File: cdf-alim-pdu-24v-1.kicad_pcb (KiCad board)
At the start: 2 copper layers, 85 x 60 mm, 130 parts, among them J1 Conn_01x02, J10 Conn_01x02, J11 Conn_01x02, J12 Conn_01x02, J13 Conn_01x02, J14 Conn_01x02, J15 Conn_01x02, J16 Conn_01x02, J17 Conn_01x02, J2 Conn_01x02, J3 Conn_01x02, J4 Conn_01x02, J5 Conn_01x02, J6 Conn_01x02, J7 Conn_01x02, J8 Conn_01x02, J9 Conn_01x02, Q1 BSC019N04LS, Q2 BSC019N04LS, Q3 BSC019N04LS, U1 TPS25983, U2 TPS25983, U3 TPS25983, U4 HT753-1, U5 MX25947, U6 MX25947, U7 MX25947

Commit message: pcb: center board
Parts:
- moved C1 56.3 mm to (114.0, 104.2)
- moved C10 56.3 mm to (115.5, 112.0)
- moved C11 56.3 mm to (123.8, 102.8)
- moved C12 56.3 mm to (146.2, 120.5)
- moved C13 56.3 mm to (146.2, 73.8)
- moved C14 56.3 mm to (154.5, 111.2)
- moved C15 56.3 mm to (154.5, 64.5)
- moved C16 56.3 mm to (137.5, 65.0)
- moved C17 56.3 mm to (137.5, 120.0)
- moved C18 56.3 mm to (137.5, 73.0)
- moved C19 56.3 mm to (137.5, 112.0)
- moved C2 56.3 mm to (144.8, 112.8)
- moved C20 56.3 mm to (117.2, 116.0)
- moved C21 56.3 mm to (129.8, 79.0)
- moved C22 56.3 mm to (129.8, 106.0)
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
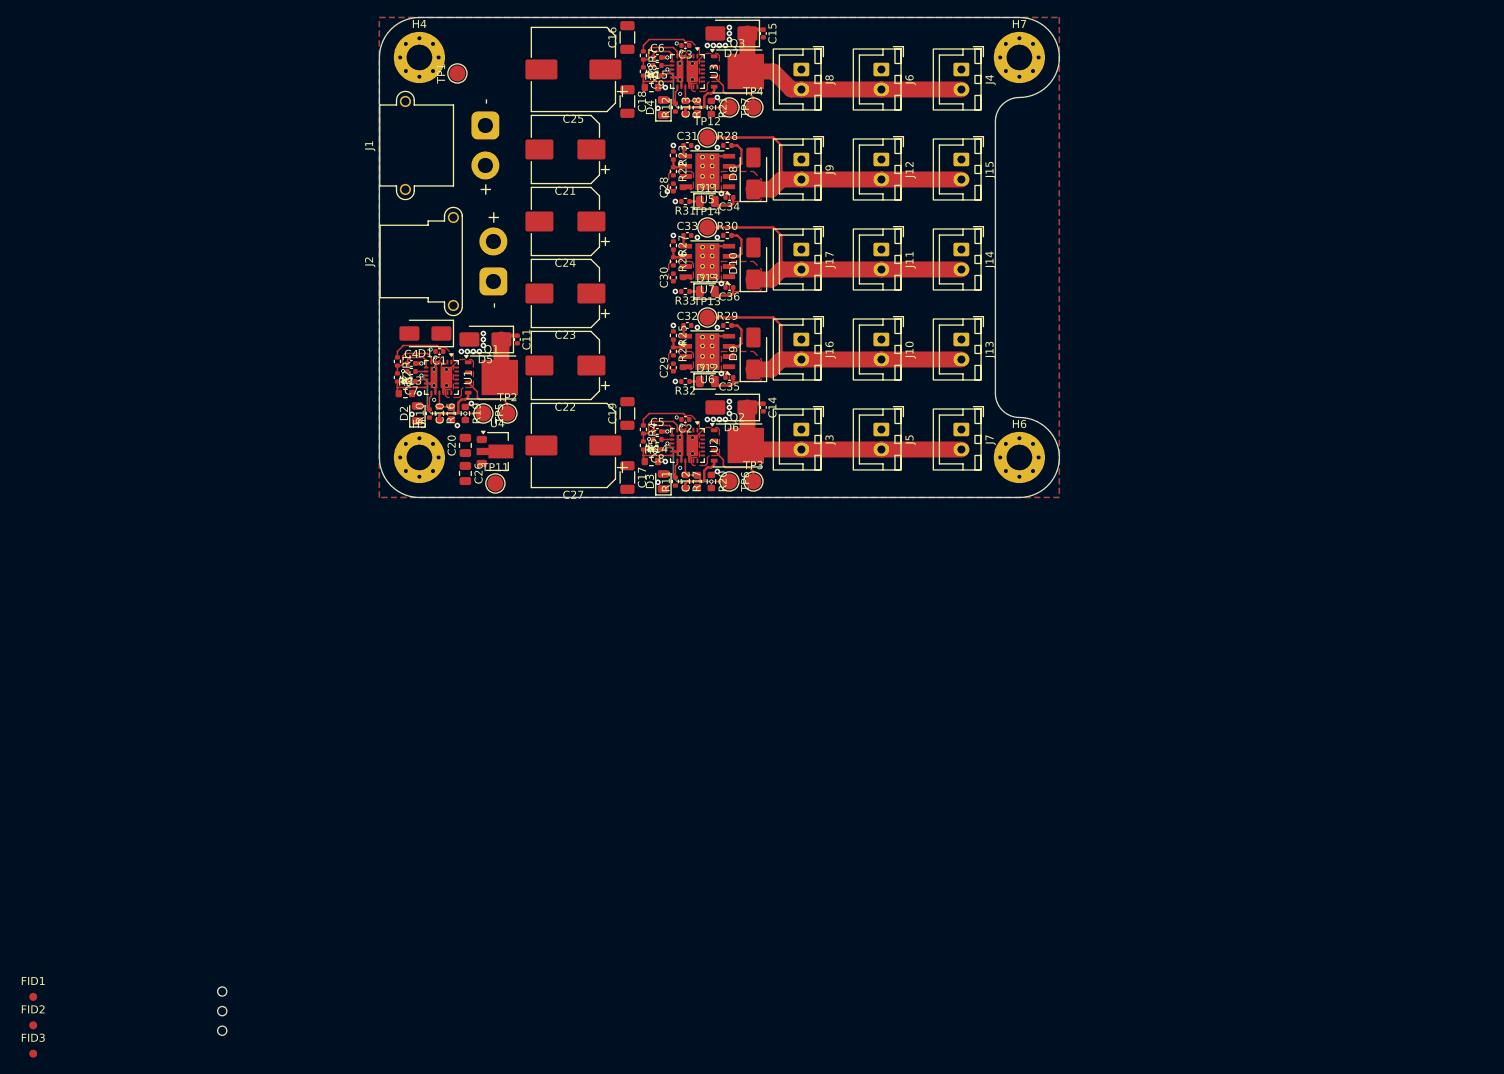
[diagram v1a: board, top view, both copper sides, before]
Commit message: pcb: place mounting holes/fiducials
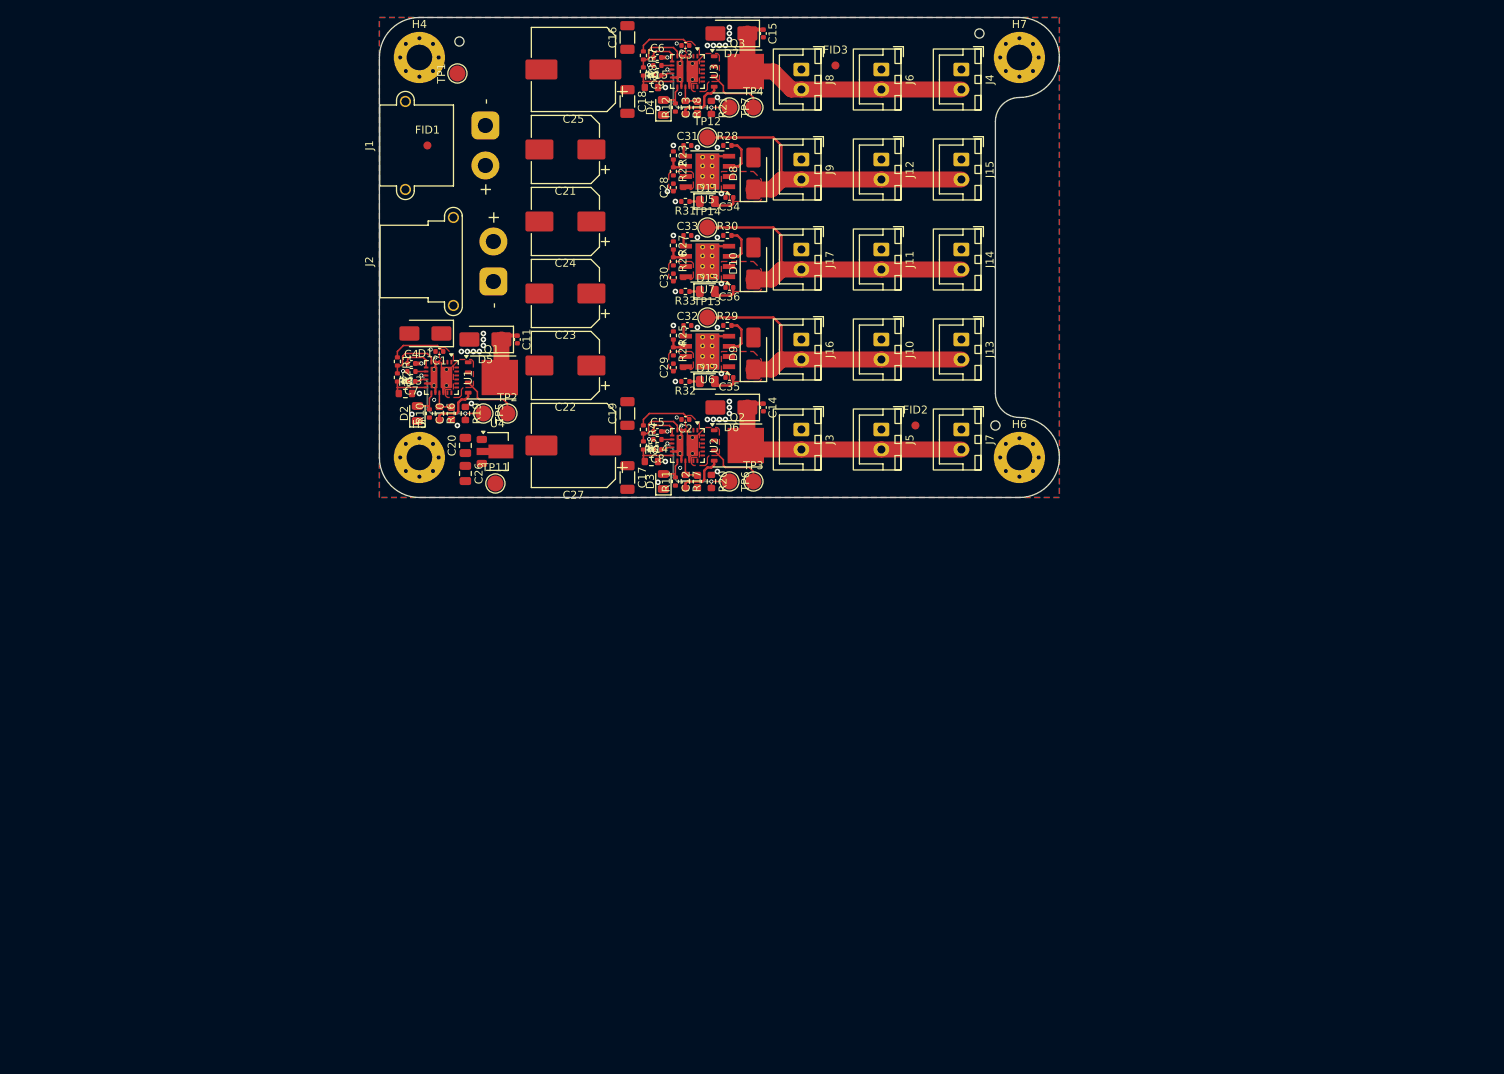
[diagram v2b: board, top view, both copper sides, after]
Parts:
- moved FID3 159.1 mm to (163.5, 68.5)
- moved H3 156.5 mm to (181.5, 64.5)
- moved FID2 133.3 mm to (173.5, 113.5)
- moved H2 124.8 mm to (116.5, 65.5)
- moved H1 119.8 mm to (183.5, 113.5)
- moved FID1 117.3 mm to (112.5, 78.5)
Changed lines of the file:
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@@
 	(footprint "Fiducial:Fiducial_1mm_Mask2mm"
 		(layer "F.Cu")
-		(at 63.225 184.925)
+		(at 112.5 78.5)
 		(descr "Fiducial, circular marking, 1mm bare copper, 2mm soldermask opening (Level A)")
 		(tags "fiducial")
@@
 	(footprint "Fiducial:Fiducial_1mm_Mask2mm"
 		(layer "F.Cu")
-		(at 63.225 192.025)
+		(at 163.5 68.5)
 		(descr "Fiducial, circular marking, 1mm bare copper, 2mm soldermask opening (Level A)")
 		(tags "fiducial")
@@
 	(footprint "MountingHole:ToolingHole_1.152mm"
 		(layer "F.Cu")
-		(at 86.855 184.255)
+		(at 183.5 113.5)
 		(descr "Tooling Hole 1.152mm, 1.3mm solder mask, JLCPCB specification, https://jlcpcb.com/help/article/How-to-add-tooling-holes-for-PCB-assembly-order")
 		(tags "mounting")
@@
 			(polygon
 				(pts
-					(xy 87.555 184.255) (xy 87.534659 184.087479) (xy 87.474819 183.929694) (xy 87.378958 183.790814)
-					(xy 87.252645 183.678911) (xy 87.103223 183.600489) (xy 86.939376 183.560104) (xy 86.770624 183.560104)
-					(xy 86.606777 183.600489) (xy 86.457355 183.678911) (xy 86.331042 183.790814) (xy 86.235181 183.929694)
-					(xy 86.175341 184.087479) (xy 86.155 184.255) (xy 86.175341 184.422521) (xy 86.235181 184.580306)
-					(xy 86.331042 184.719186) (xy 86.457355 184.831089) (xy 86.606777 184.909511) (xy 86.770624 184.949896)
-					(xy 86.939376 184.949896) (xy 87.103223 184.909511) (xy 87.252645 184.831089) (xy 87.378958 184.719186)
-					(xy 87.474819 184.580306) (xy 87.534659 184.422521)
+					(xy 184.2 113.5) (xy 184.179659 113.332479) (xy 184.119819 113.174694) (xy 184.023958 113.035814)
+					(xy 183.897645 112.923911) (xy 183.748223 112.845489) (xy 183.584376 112.805104) (xy 183.415624 112.805104)
+					(xy 183.251777 112.845489) (xy 183.102355 112.923911) (xy 182.976042 113.035814) (xy 182.880181 113.174694)
+					(xy 182.820341 113.332479) (xy 182.8 113.5) (xy 182.820341 113.667521) (xy 182.880181 113.825306)
+					(xy 182.976042 113.964186) (xy 183.102355 114.076089) (xy 183.251777 114.154511) (xy 183.415624 114.194896)
+					(xy 183.584376 114.194896) (xy 183.748223 114.154511) (xy 183.897645 114.076089) (xy 184.023958 113.964186)
+					(xy 184.119819 113.825306) (xy 184.179659 113.667521)
 				)
 			)
@@
 	(footprint "MountingHole:ToolingHole_1.152mm"
 		(layer "F.Cu")
-		(at 86.855 189.155)
+		(at 181.5 64.5)
 		(descr "Tooling Hole 1.152mm, 1.3mm solder mask, JLCPCB specification, https://jlcpcb.com/help/article/How-to-add-tooling-holes-for-PCB-assembly-order")
 		(tags "mounting")
@@
 			(polygon
 				(pts
-					(xy 87.555 189.155) (xy 87.534659 188.987479) (xy 87.474819 188.829694) (xy 87.378958 188.690814)
-					(xy 87.252645 188.578911) (xy 87.103223 188.500489) (xy 86.939376 188.460104) (xy 86.770624 188.460104)
-					(xy 86.606777 188.500489) (xy 86.457355 188.578911) (xy 86.331042 188.690814) (xy 86.235181 188.829694)
-					(xy 86.175341 188.987479) (xy 86.155 189.155) (xy 86.175341 189.322521) (xy 86.235181 189.480306)
-					(xy 86.331042 189.619186) (xy 86.457355 189.731089) (xy 86.606777 189.809511) (xy 86.770624 189.849896)
-					(xy 86.939376 189.849896) (xy 87.103223 189.809511) (xy 87.252645 189.731089) (xy 87.378958 189.619186)
-					(xy 87.474819 189.480306) (xy 87.534659 189.322521)
+					(xy 182.2 64.5) (xy 182.179659 64.332479) (xy 182.119819 64.174694) (xy 182.023958 64.035814) (xy 181.897645 63.923911)
+					(xy 181.748223 63.845489) (xy 181.584376 63.805104) (xy 181.415624 63.805104) (xy 181.251777 63.845489)
+					(xy 181.102355 63.923911) (xy 180.976042 64.035814) (xy 180.880181 64.174694) (xy 180.820341 64.332479)
+					(xy 180.8 64.5) (xy 180.820341 64.667521) (xy 180.880181 64.825306) (xy 180.976042 64.964186) (xy 181.102355 65.076089)
+					(xy 181.251777 65.154511) (xy 181.415624 65.194896) (xy 181.584376 65.194896) (xy 181.748223 65.154511)
+					(xy 181.897645 65.076089) (xy 182.023958 64.964186) (xy 182.119819 64.825306) (xy 182.179659 64.667521)
 				)
 			)
@@
 	(footprint "MountingHole:ToolingHole_1.152mm"
 		(layer "F.Cu")
-		(at 86.855 186.705)
+		(at 116.5 65.5)
 		(descr "Tooling Hole 1.152mm, 1.3mm solder mask, JLCPCB specification, https://jlcpcb.com/help/article/How-to-add-tooling-holes-for-PCB-assembly-order")
 		(tags "mounting")
@@
 			(polygon
 				(pts
-					(xy 87.555 186.705) (xy 87.534659 186.537479) (xy 87.474819 186.379694) (xy 87.378958 186.240814)
-					(xy 87.252645 186.128911) (xy 87.103223 186.050489) (xy 86.939376 186.010104) (xy 86.770624 186.010104)
-					(xy 86.606777 186.050489) (xy 86.457355 186.128911) (xy 86.331042 186.240814) (xy 86.235181 186.379694)
-					(xy 86.175341 186.537479) (xy 86.155 186.705) (xy 86.175341 186.872521) (xy 86.235181 187.030306)
-					(xy 86.331042 187.169186) (xy 86.457355 187.281089) (xy 86.606777 187.359511) (xy 86.770624 187.399896)
-					(xy 86.939376 187.399896) (xy 87.103223 187.359511) (xy 87.252645 187.281089) (xy 87.378958 187.169186)
-					(xy 87.474819 187.030306) (xy 87.534659 186.872521)
+					(xy 117.2 65.5) (xy 117.179659 65.332479) (xy 117.119819 65.174694) (xy 117.023958 65.035814) (xy 116.897645 64.923911)
+					(xy 116.748223 64.845489) (xy 116.584376 64.805104) (xy 116.415624 64.805104) (xy 116.251777 64.845489)
+					(xy 116.102355 64.923911) (xy 115.976042 65.035814) (xy 115.880181 65.174694) (xy 115.820341 65.332479)
+					(xy 115.8 65.5) (xy 115.820341 65.667521) (xy 115.880181 65.825306) (xy 115.976042 65.964186) (xy 116.102355 66.076089)
+					(xy 116.251777 66.154511) (xy 116.415624 66.194896) (xy 116.584376 66.194896) (xy 116.748223 66.154511)
+					(xy 116.897645 66.076089) (xy 117.023958 65.964186) (xy 117.119819 65.825306) (xy 117.179659 65.667521)
 				)
 			)
@@
 	(footprint "Fiducial:Fiducial_1mm_Mask2mm"
 		(layer "F.Cu")
-		(at 63.225 188.475)
+		(at 173.5 113.5)
 		(descr "Fiducial, circular marking, 1mm bare copper, 2mm soldermask opening (Level A)")
 		(tags "fiducial")

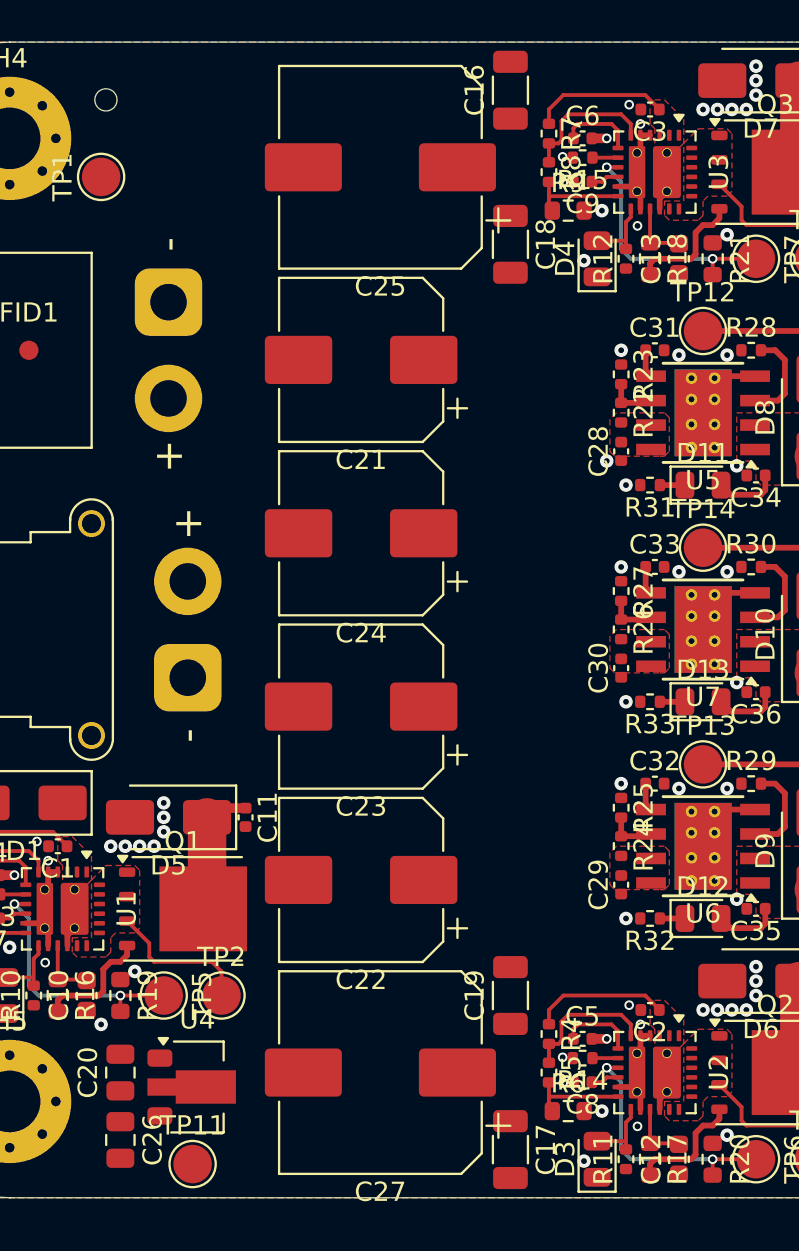
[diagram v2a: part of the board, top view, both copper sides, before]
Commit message: pcb: add +24v routing
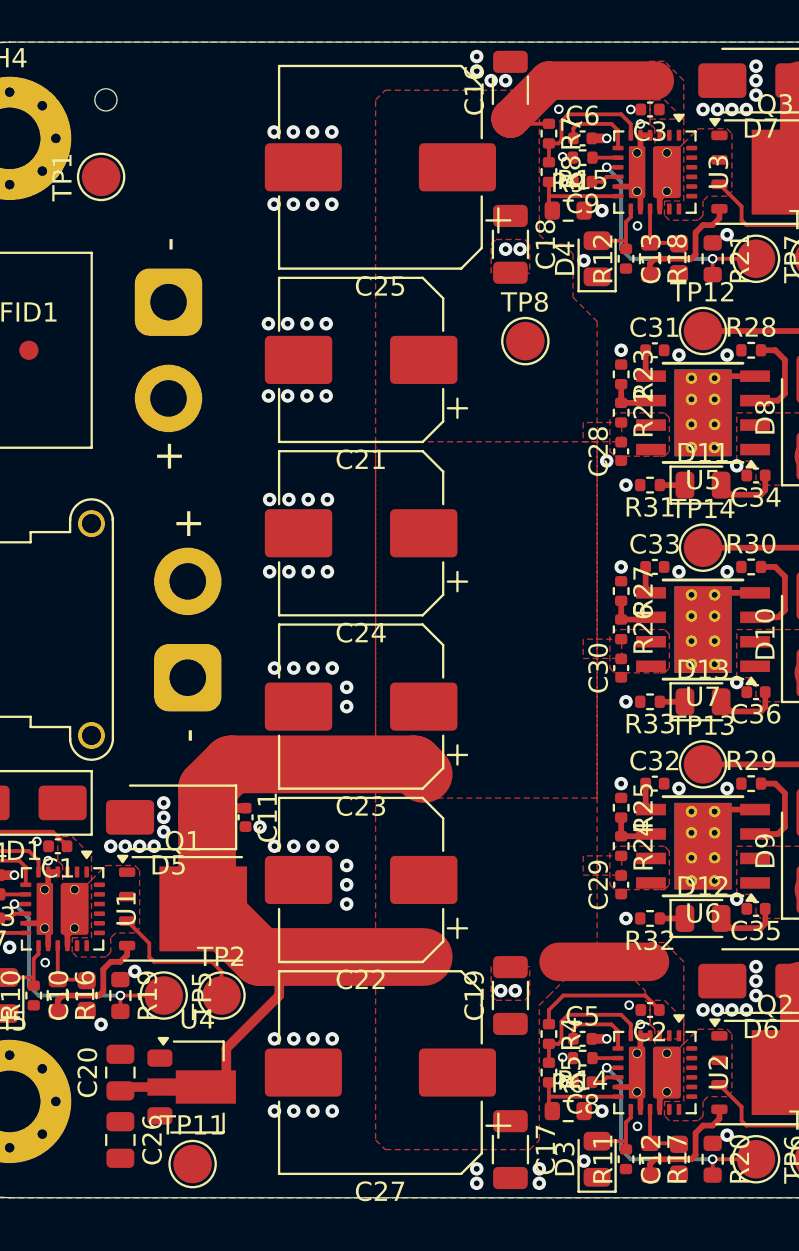
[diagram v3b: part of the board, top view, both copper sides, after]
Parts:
- added TP8: TestPoint, TestPoint:TestPoint_Pad_D2.0mm, F.Cu at (138.3, 78.0)
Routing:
- net +24V: track 23.4 -> 70.1 mm
- net GND: vias 65 -> 124

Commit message: pcb: fix connectors thermal reliefs
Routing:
- net GND: vias 124 -> 141
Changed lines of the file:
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@@
 			(pinfunction "Pin_1_1")
 			(pintype "passive")
+			(thermal_bridge_width 1)
 		)
 		(pad "2" thru_hole oval
@@
 			(pinfunction "Pin_1_1")
 			(pintype "passive")
+			(thermal_bridge_width 1)
 		)
 		(pad "2" thru_hole oval
@@
 			(pinfunction "Pin_1_1")
 			(pintype "passive")
+			(thermal_bridge_width 1)
 		)
 		(pad "2" thru_hole oval
@@
 			(pinfunction "Pin_1_1")
 			(pintype "passive")
+			(thermal_bridge_width 1)
 		)
 		(pad "2" thru_hole oval
@@
 			(pinfunction "Pin_1_1")
 			(pintype "passive")
+			(thermal_bridge_width 1)
 		)
 		(pad "2" thru_hole oval
@@
 			(pinfunction "Pin_1_1")
 			(pintype "passive")
+			(thermal_bridge_width 1)
 		)
 		(pad "2" thru_hole oval
@@
 			(pinfunction "Pin_1_1")
 			(pintype "passive")
+			(thermal_bridge_width 1)
 		)
 		(pad "2" thru_hole oval
@@
 			(pinfunction "Pin_1_1")
 			(pintype "passive")
+			(thermal_bridge_width 1)
 		)
 		(pad "2" thru_hole oval
@@
 			(pinfunction "Pin_1_1")
 			(pintype "passive")
+			(thermal_bridge_width 1)
 		)
 		(pad "2" thru_hole oval
@@
 			(pinfunction "Pin_1_1")
 			(pintype "passive")
+			(thermal_bridge_width 1)
 		)
 		(pad "2" thru_hole oval
@@
 			(pinfunction "Pin_1_1")
 			(pintype "passive")
+			(thermal_bridge_width 1)
 		)
 		(pad "2" thru_hole oval
@@
 			(pinfunction "Pin_1_1")
 			(pintype "passive")
+			(thermal_bridge_width 1)
 		)
 		(pad "2" thru_hole oval
@@
 			(pinfunction "Pin_1_1")
 			(pintype "passive")
+			(thermal_bridge_width 1)
 		)
 		(pad "2" thru_hole oval
@@
 			(pinfunction "Pin_1_1")
 			(pintype "passive")
+			(thermal_bridge_width 1)
 		)
 		(pad "2" thru_hole oval
@@
 			(pinfunction "Pin_1_1")
 			(pintype "passive")
+			(thermal_bridge_width 1)
 		)
 		(pad "2" thru_hole oval
@@
 	)
 	(via
+		(at 154.75 103.5)
+		(size 0.7)
+		(drill 0.3)
+		(layers "F.Cu" "B.Cu")
+		(free yes)
+		(net "GND")
+	)
+	(via
 		(at 116.75 104.25)
 		(size 0.7)
@@
 	)
 	(via
+		(at 154.75 80.25)
+		(size 0.7)
+		(drill 0.3)
+		(layers "F.Cu" "B.Cu")
+		(free yes)
+		(net "GND")
+	)
+	(via
 		(at 137.75 111.75)
 		(size 0.7)
@@
 	)
 	(via
+		(at 154.75 78.75)
+		(size 0.7)
+		(drill 0.3)
+		(layers "F.Cu" "B.Cu")
+		(free yes)
+		(net "GND")
+	)
+	(via
 		(at 118 110.75)
 		(size 0.7)
@@
 	)
 	(via
+		(at 151.025835 102.80114)
+		(size 0.5)
+		(drill 0.3)
+		(layers "F.Cu" "B.Cu")
+		(free yes)
+		(net "GND")
+	)
+	(via
+		(at 154.75 102)
+		(size 0.7)
+		(drill 0.3)
+		(layers "F.Cu" "B.Cu")
+		(free yes)
+		(net "GND")
+	)
+	(via
 		(at 110.569005 112.096526)
 		(size 0.7)
@@
 	)
 	(via
+		(at 154.75 79.5)
+		(size 0.7)
+		(drill 0.3)
+		(layers "F.Cu" "B.Cu")
+		(free yes)
+		(net "GND")
+	)
+	(via
 		(at 124.5 103.25)
 		(size 0.7)
@@
 	)
 	(via
+		(at 154.75 90.75)
+		(size 0.7)
+		(drill 0.3)
+		(layers "F.Cu" "B.Cu")
+		(free yes)
+		(net "GND")
+	)
+	(via
 		(at 147.5 66)
 		(size 0.7)
@@
 	)
 	(via
+		(at 154.75 101.25)
+		(size 0.7)
+		(drill 0.3)
+		(layers "F.Cu" "B.Cu")
+		(free yes)
+		(net "GND")
+	)
+	(via
 		(at 128.229339 67.16822)
 		(size 0.7)
@@
 	)
 	(via
+		(at 154.75 102.75)
+		(size 0.7)
+		(drill 0.3)
+		(layers "F.Cu" "B.Cu")
+		(free yes)
+		(net "GND")
+	)
+	(via
 		(at 135.75 64)
 		(size 0.7)
@@
 	)
 	(via
+		(at 149.672719 80.318028)
+		(size 0.5)
+		(drill 0.3)
+		(layers "F.Cu" "B.Cu")
+		(free yes)
+		(net "GND")
+	)
+	(via
 		(at 125 90)
 		(size 0.7)
@@
 	)
 	(via
+		(at 154.75 92.25)
+		(size 0.7)
+		(drill 0.3)
+		(layers "F.Cu" "B.Cu")
+		(free yes)
+		(net "GND")
+	)
+	(via
 		(at 111.5 109.5)
 		(size 0.7)
@@
 	)
 	(via
+		(at 154.75 91.5)
+		(size 0.7)
+		(drill 0.3)
+		(layers "F.Cu" "B.Cu")
+		(free yes)
+		(net "GND")
+	)
+	(via
 		(at 143.25 101)
 		(size 0.7)
@@
 	)
 	(via
+		(at 154.75 81)
+		(size 0.7)
+		(drill 0.3)
+		(layers "F.Cu" "B.Cu")
+		(free yes)
+		(net "GND")
+	)
+	(via
 		(at 150.25 64.5)
 		(size 0.7)
@@
 	)
 	(via
+		(at 151.020136 80.278399)
+		(size 0.5)
+		(drill 0.3)
+		(layers "F.Cu" "B.Cu")
+		(free yes)
+		(net "GND")
+	)
+	(via
 		(at 148.75 78.75)
 		(size 0.7)
@@
 	)
 	(via
+		(at 151.106006 91.604739)
+		(size 0.5)
+		(drill 0.3)
+		(layers "F.Cu" "B.Cu")
+		(free yes)
+		(net "GND")
+	)
+	(via
+		(at 154.75 90)
+		(size 0.7)
+		(drill 0.3)
+		(layers "F.Cu" "B.Cu")
+		(free yes)
+		(net "GND")
+	)
+	(via
 		(at 144.25 113.5)
 		(size 0.5)
@@
 		(drill 0.3)
 		(layers "F.Cu" "B.Cu")
+		(free yes)
+		(net "GND")
+	)
+	(via
+		(at 149.615921 91.620591)
+		(size 0.5)
+		(drill 0.3)
+		(layers "F.Cu" "B.Cu")
